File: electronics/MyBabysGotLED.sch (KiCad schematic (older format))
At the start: 16 parts, among them J1 APA102, J2 WS2812, J3 Serial, P3 ATX_Power_2x12_Connector, Q1 PZT2222A, U2 SN74AHCT125, U3 LM1117-3.3

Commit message: Most of BoM details added.  Part of #4
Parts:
- C1: Farnell (none) -> 2326201; Farnell Price/Stock (none) -> https://uk.farnell.com/panasonic/eeefk1e102aq/cap-1000-f-25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
- C3: value 100nF -> 0.1uF; Farnell (none) -> 1759038RL; Farnell Price/Stock (none) -> https://uk.farnell.com/multicomp/mc0603f104z250ct/cap-0-1-f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
- C4: footprint Capacitor_SMD:C_0603_1608Metric_Pad1.05x0.95mm_HandSolder -> Capacitor_SMD:C_1206_3216Metric_Pad1.42x1.75mm_HandSolder; Farnell (none) -> 2320887RL; Farnell Price/Stock (none) -> https://uk.farnell.com/multicomp/mc1206x106k250ct/cap-10-f-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
- C5: Farnell (none) -> 1759038RL; Farnell Price/Stock (none) -> https://uk.farnell.com/multicomp/mc0603f104z250ct/cap-0-1-f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
- F1: Farnell (none) -> 1861167RL; Farnell Price/Stock (none) -> https://uk.farnell.com/multicomp/mc36225/fuse-ptc-reset-smd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
- J3: Description (none) -> DNP
- Q1: value PZT2222A -> NJT4031NT1G; Farnell (none) -> 2533335; Farnell Price/Stock (none) -> https://uk.farnell.com/on-semiconductor/njt4031nt1g/transis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
- R3, R4, R5: Farnell (none) -> 2502462; Farnell Price/Stock (none) -> https://uk.farnell.com/walsin/wr06x4700ftl/res-470r-1-75v-0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
- U2: Farnell (none) -> 3006129; Farnell Price/Stock (none) -> https://uk.farnell.com/texas-instruments/sn74ahct125d/ic-bu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
- U3: Farnell (none) -> 1202826RL; Farnell Price/Stock (none) -> https://uk.farnell.com/stmicroelectronics/ld1117s33tr/v-reg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
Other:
- moved on the sheet: Q1
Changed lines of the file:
@@
 F 2 "Package_SO:SOIC-14_3.9x8.7mm_P1.27mm" H 4250 4600 50  0001 C CNN
 F 3 "https://www.ti.com/lit/ds/symlink/sn74ahct125.pdf" H 4250 4600 50  0001 C CNN
+F 4 "3006129" H 4250 4600 50  0001 C CNN "Farnell"
+F 5 "https://uk.farnell.com/texas-instruments/sn74ahct125d/ic-buffer-gate-quad-3state-smd/dp/3006129" H 4250 4600 50  0001 C CNN "Farnell Price/Stock"
 	1    4250 4600
 	1    0    0    -1
@@
 F 2 "Capacitor_SMD:C_0603_1608Metric_Pad1.05x0.95mm_HandSolder" H 5388 4400 50  0001 C CNN
 F 3 "~" H 5350 4550 50  0001 C CNN
+F 4 "1759038RL" H 5350 4550 50  0001 C CNN "Farnell"
+F 5 "https://uk.farnell.com/multicomp/mc0603f104z250ct/cap-0-1-f-25v-y5v-0603/dp/1759038RL" H 5350 4550 50  0001 C CNN "Farnell Price/Stock"
 	1    5350 4550
 	1    0    0    -1
@@
 F 2 "Resistor_SMD:R_0603_1608Metric_Pad1.05x0.95mm_HandSolder" V 2980 4800 50  0001 C CNN
 F 3 "~" H 3050 4800 50  0001 C CNN
+F 4 "2502462" V 3050 4800 50  0001 C CNN "Farnell"
+F 5 "https://uk.farnell.com/walsin/wr06x4700ftl/res-470r-1-75v-0603-thick-film/dp/2502462" V 3050 4800 50  0001 C CNN "Farnell Price/Stock"
 	1    3050 4800
 	0    1    1    0
@@
 F 2 "Resistor_SMD:R_0603_1608Metric_Pad1.05x0.95mm_HandSolder" V 2980 4500 50  0001 C CNN
 F 3 "~" H 3050 4500 50  0001 C CNN
+F 4 "2502462" V 3050 4500 50  0001 C CNN "Farnell"
+F 5 "https://uk.farnell.com/walsin/wr06x4700ftl/res-470r-1-75v-0603-thick-film/dp/2502462" V 3050 4500 50  0001 C CNN "Farnell Price/Stock"
 	1    3050 4500
 	0    1    1    0
@@
 F 2 "Connector_PinHeader_2.54mm:PinHeader_1x06_P2.54mm_Vertical" H 6650 1150 50  0001 C CNN
 F 3 "~" H 6650 1150 50  0001 C CNN
+F 4 "DNP" H 6650 1150 50  0001 C CNN "Description"
 	1    6650 1150
 	0    -1   -1   0
@@
 F 2 "Package_TO_SOT_SMD:SOT-223-3_TabPin2" H 4550 1800 50  0001 C CNN
 F 3 "http://www.ti.com/lit/ds/symlink/lm1117.pdf" H 4550 1800 50  0001 C CNN
+F 4 "1202826RL" H 4550 1800 50  0001 C CNN "Farnell"
+F 5 "https://uk.farnell.com/stmicroelectronics/ld1117s33tr/v-reg-ldo-3-3v-smd-1117-sot-223/dp/1202826RL" H 4550 1800 50  0001 C CNN "Farnell Price/Stock"
 	1    4550 1800
 	1    0    0    -1
@@
 P 3900 1950
 F 0 "C3" H 4015 1996 50  0000 L CNN
-F 1 "100nF" H 4015 1905 50  0000 L CNN
+F 1 "0.1uF" H 4015 1905 50  0000 L CNN
 F 2 "Capacitor_SMD:C_0603_1608Metric_Pad1.05x0.95mm_HandSolder" H 3938 1800 50  0001 C CNN
 F 3 "~" H 3900 1950 50  0001 C CNN
+F 4 "1759038RL" H 3900 1950 50  0001 C CNN "Farnell"
+F 5 "https://uk.farnell.com/multicomp/mc0603f104z250ct/cap-0-1-f-25v-y5v-0603/dp/1759038RL" H 3900 1950 50  0001 C CNN "Farnell Price/Stock"
 	1    3900 1950
 	1    0    0    -1
@@
 F 0 "C4" H 5215 1996 50  0000 L CNN
 F 1 "10uF" H 5215 1905 50  0000 L CNN
-F 2 "Capacitor_SMD:C_0603_1608Metric_Pad1.05x0.95mm_HandSolder" H 5138 1800 50  0001 C CNN
+F 2 "Capacitor_SMD:C_1206_3216Metric_Pad1.42x1.75mm_HandSolder" H 5138 1800 50  0001 C CNN
 F 3 "~" H 5100 1950 50  0001 C CNN
+F 4 "2320887RL" H 5100 1950 50  0001 C CNN "Farnell"
+F 5 "https://uk.farnell.com/multicomp/mc1206x106k250ct/cap-10-f-25v-10-x5r-1206/dp/2320887RL" H 5100 1950 50  0001 C CNN "Farnell Price/Stock"
 	1    5100 1950
 	1    0    0    -1
@@
 Wire Wire Line
 	3900 2100 3900 2700
-Wire Wire Line
-	3900 2700 3300 2700
 Connection ~ 3900 2100
 Connection ~ 2400 2700
@@
 F 2 "mcqn-kicad-lib:c_elec_12.5x12.5" H 1838 4300 50  0001 C CNN
 F 3 "~" H 1800 4450 50  0001 C CNN
+F 4 "2326201" H 1800 4450 50  0001 C CNN "Farnell"
+F 5 "https://uk.farnell.com/panasonic/eeefk1e102aq/cap-1000-f-25v-radial-smd/dp/2326201" H 1800 4450 50  0001 C CNN "Farnell Price/Stock"
 	1    1800 4450
 	1    0    0    -1
@@
 F 2 "Resistor_SMD:R_0603_1608Metric_Pad1.05x0.95mm_HandSolder" V 4280 2400 50  0001 C CNN
 F 3 "~" H 4350 2400 50  0001 C CNN
+F 4 "2502462" V 4350 2400 50  0001 C CNN "Farnell"
+F 5 "https://uk.farnell.com/walsin/wr06x4700ftl/res-470r-1-75v-0603-thick-film/dp/2502462" V 4350 2400 50  0001 C CNN "Farnell Price/Stock"
 	1    4350 2400
 	0    1    1    0
@@
 L Transistor_BJT:PZT2222A Q1
 U 1 1 5F963FC6
-P 3400 2400
-F 0 "Q1" H 3591 2446 50  0000 L CNN
-F 1 "PZT2222A" H 3591 2355 50  0000 L CNN
-F 2 "Package_TO_SOT_SMD:SOT-223-3_TabPin2" H 3600 2325 50  0001 L CIN
-F 3 "http://www.fairchildsemi.com/ds/PN/PN2222A.pdf" H 3400 2400 50  0001 L CNN
-	1    3400 2400
+P 3550 2400
+F 0 "Q1" H 3741 2446 50  0000 L CNN
+F 1 "NJT4031NT1G" H 3741 2355 50  0000 L CNN
+F 2 "Package_TO_SOT_SMD:SOT-223-3_TabPin2" H 3750 2325 50  0001 L CIN
+F 3 "http://www.fairchildsemi.com/ds/PN/PN2222A.pdf" H 3550 2400 50  0001 L CNN
+F 4 "2533335" H 3550 2400 50  0001 C CNN "Farnell"
+F 5 "https://uk.farnell.com/on-semiconductor/njt4031nt1g/transistor-bipol-npn-40v/dp/2533335" H 3550 2400 50  0001 C CNN "Farnell Price/Stock"
+	1    3550 2400
 	-1   0    0    -1
 $EndComp
-Wire Wire Line
-	2850 2100 3300 2100
-Wire Wire Line
-	3300 2100 3300 2200
-Wire Wire Line
-	3300 2600 3300 2700
-Connection ~ 3300 2700
-Wire Wire Line
-	3300 2700 2400 2700
-Wire Wire Line
-	3600 2400 4200 2400
 Wire Wire Line
 	4500 2400 7950 2400
@@
 F 2 "Fuse:Fuse_1812_4532Metric_Pad1.30x3.40mm_HandSolder" H 3350 1600 50  0001 L CNN
 F 3 "~" H 3300 1800 50  0001 C CNN
+F 4 "1861167RL" V 3300 1800 50  0001 C CNN "Farnell"
+F 5 "https://uk.farnell.com/multicomp/mc36225/fuse-ptc-reset-smd-24v-1-1a/dp/1861167RL" V 3300 1800 50  0001 C CNN "Farnell Price/Stock"
 	1    3300 1800
 	0    1    1    0
@@
 Wire Wire Line
 	3050 1800 3150 1800
+Wire Wire Line
+	2400 2700 3450 2700
+Wire Wire Line
+	4200 2400 3750 2400
+Wire Wire Line
+	3450 2200 3450 2100
+Wire Wire Line
+	2850 2100 3450 2100
+Wire Wire Line
+	3450 2600 3450 2700
+Connection ~ 3450 2700
+Wire Wire Line
+	3450 2700 3900 2700
 $EndSCHEMATC

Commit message: PCB laid out.  Final part of #3 and all of #5
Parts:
- F2: footprint (none) -> mcqn-kicad-lib:Keystone_3557-2_Blade_Fuseholder; Digikey (none) -> 36-3557-2-ND; Digikey Price/Stock (none) -> https://www.digikey.co.uk/product-detail/en/keystone-electr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; Farnell (none) -> 2292904; Farnell Price/Stock (none) -> https://uk.farnell.com/keystone/3557-2/fuse-holder-0-8x2-8m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
- J1: footprint Connector_Phoenix_MSTB:PhoenixContact_MSTBVA_2,5_5-G-5,08_1x05_P5.08mm_Vertical -> Connector_Phoenix_MSTB:PhoenixContact_MSTBVA_2,5_4-G-5,08_1x04_P5.08mm_Vertical
- J2: footprint (none) -> Connector_PinHeader_2.54mm:PinHeader_1x03_P2.54mm_Vertical; Farnell (none) -> 1593412; Farnell Price/Stock (none) -> https://uk.farnell.com/multicomp/2211s-03g/header-1-row-ver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
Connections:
- net GND: now also J1.1 (Pin_1); no longer J1.4 (Pin_4)
- net LED_Clk: now also U2.2 (1A); no longer U2.5 (2A)
- net LED_Data: now also U2.5 (2A); no longer U2.2 (1A)
- net at C1.1, C5.1, F2.2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: now also J1.4 (Pin_4); no longer J1.1 (Pin_1)
- net at J1.2 (Pin_2), J2.2 (Pin_2): now also R4.2; no longer R3.2
- net at J1.3 (Pin_3): now also R3.2; no longer R4.2
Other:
- moved on the sheet: C1, J2
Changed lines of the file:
@@
 L Connector_Generic:Conn_01x03 J2
 U 1 1 5F8EED32
-P 2350 4500
-F 0 "J2" H 2268 4817 50  0000 C CNN
-F 1 "WS2812" H 2268 4726 50  0000 C CNN
-F 2 "" H 2350 4500 50  0001 C CNN
-F 3 "~" H 2350 4500 50  0001 C CNN
-	1    2350 4500
+P 2350 4800
+F 0 "J2" H 2268 5117 50  0000 C CNN
+F 1 "WS2812" H 2268 5026 50  0000 C CNN
+F 2 "Connector_PinHeader_2.54mm:PinHeader_1x03_P2.54mm_Vertical" H 2350 4800 50  0001 C CNN
+F 3 "~" H 2350 4800 50  0001 C CNN
+F 4 "1593412" H 2350 4800 50  0001 C CNN "Farnell"
+F 5 "https://uk.farnell.com/multicomp/2211s-03g/header-1-row-vert-3way/dp/1593412" H 2350 4800 50  0001 C CNN "Farnell Price/Stock"
+	1    2350 4800
 	-1   0    0    -1
 $EndComp
-$Comp
-L Connector_Generic:Conn_01x04 J1
-U 1 1 5F8F55BB
-P 1200 4500
-F 0 "J1" H 1118 4817 50  0000 C CNN
-F 1 "APA102" H 1118 4726 50  0000 C CNN
-F 2 "Connector_Phoenix_MSTB:PhoenixContact_MSTBVA_2,5_5-G-5,08_1x05_P5.08mm_Vertical" H 1200 4500 50  0001 C CNN
-F 3 "~" H 1200 4500 50  0001 C CNN
-F 4 "2517880" H 1200 4500 50  0001 C CNN "Farnell"
-F 5 "https://uk.farnell.com/imo-precision-controls/21-95mv-4-e/terminal-block-header-4pos-th/dp/2517880" H 1200 4500 50  0001 C CNN "Farnell Price/Stock"
-	1    1200 4500
-	-1   0    0    -1
-$EndComp
-Wire Wire Line
-	2800 3900 2800 4400
-Wire Wire Line
-	2800 4400 2550 4400
 Wire Wire Line
 	1600 3900 1600 4400
@@
 	1600 4400 1400 4400
 Wire Wire Line
-	2550 4500 2800 4500
-Wire Wire Line
 	1400 4600 1500 4600
-Wire Wire Line
-	1500 4600 1500 4800
-Wire Wire Line
-	1400 4500 1600 4500
-Wire Wire Line
-	1600 4500 1600 4700
-Wire Wire Line
-	2800 4700 2800 4500
 $Comp
 L Device:C C5
@@
 $EndComp
 Wire Wire Line
-	2800 4500 2900 4500
-Connection ~ 2800 4500
-Wire Wire Line
 	1400 4700 1400 5200
 Wire Wire Line
@@
 	5350 3900 5350 4300
 Connection ~ 5350 4300
-Wire Wire Line
-	2550 4600 2550 5200
 Wire Wire Line
 	3900 4300 3800 4300
@@
 U 1 1 5F90A6A8
 P 4550 1800
+AR Path="/5F90A6A8" Ref="U3"  Part="1"
+AR Path="/5F8DAD46/5F90A6A8" Ref="U3"  Part="1"
 F 0 "U3" H 4550 2042 50  0000 C CNN
 F 1 "LM1117-3.3" H 4550 1951 50  0000 C CNN
@@
 L Device:CP C1
 U 1 1 5F942FA9
-P 1800 4450
-F 0 "C1" H 1918 4496 50  0000 L CNN
-F 1 "1000uF" H 1918 4405 50  0000 L CNN
-F 2 "mcqn-kicad-lib:c_elec_12.5x12.5" H 1838 4300 50  0001 C CNN
-F 3 "~" H 1800 4450 50  0001 C CNN
-F 4 "2326201" H 1800 4450 50  0001 C CNN "Farnell"
-F 5 "https://uk.farnell.com/panasonic/eeefk1e102aq/cap-1000-f-25v-radial-smd/dp/2326201" H 1800 4450 50  0001 C CNN "Farnell Price/Stock"
-	1    1800 4450
-	1    0    0    -1
-$EndComp
-Wire Wire Line
-	1600 3900 1800 3900
-Wire Wire Line
-	1600 4700 2800 4700
-Wire Wire Line
-	1500 4800 2900 4800
-Wire Wire Line
-	1400 5200 1800 5200
-Connection ~ 1800 3900
-Wire Wire Line
-	1800 3900 2800 3900
-Wire Wire Line
-	1800 3900 1800 4300
-Wire Wire Line
-	1800 4600 1800 5200
-Connection ~ 1800 5200
-Wire Wire Line
-	1800 5200 2550 5200
+P 1850 4250
+F 0 "C1" H 1968 4296 50  0000 L CNN
+F 1 "1000uF" H 1968 4205 50  0000 L CNN
+F 2 "mcqn-kicad-lib:c_elec_12.5x12.5" H 1888 4100 50  0001 C CNN
+F 3 "~" H 1850 4250 50  0001 C CNN
+F 4 "2326201" H 1850 4250 50  0001 C CNN "Farnell"
+F 5 "https://uk.farnell.com/panasonic/eeefk1e102aq/cap-1000-f-25v-radial-smd/dp/2326201" H 1850 4250 50  0001 C CNN "Farnell Price/Stock"
+	1    1850 4250
+	1    0    0    -1
+$EndComp
 $Comp
 L Device:R R5
@@
 Wire Wire Line
 	3200 4500 3900 4500
-Connection ~ 2800 3900
 $Comp
 L Device:Fuse F2
@@
 F 0 "F2" H 4910 3696 50  0000 L CNN
 F 1 "Fuse" H 4910 3605 50  0000 L CNN
-F 2 "" V 4780 3650 50  0001 C CNN
+F 2 "mcqn-kicad-lib:Keystone_3557-2_Blade_Fuseholder" V 4780 3650 50  0001 C CNN
 F 3 "~" H 4850 3650 50  0001 C CNN
+F 4 "2292904" H 4850 3650 50  0001 C CNN "Farnell"
+F 5 "https://uk.farnell.com/keystone/3557-2/fuse-holder-0-8x2-8mm-pcb-mount/dp/2292904" H 4850 3650 50  0001 C CNN "Farnell Price/Stock"
+F 6 "36-3557-2-ND" H 4850 3650 50  0001 C CNN "Digikey"
+F 7 "https://www.digikey.co.uk/product-detail/en/keystone-electronics/3557-2/36-3557-2-ND/2137305" H 4850 3650 50  0001 C CNN "Digikey Price/Stock"
 	1    4850 3650
 	1    0    0    -1
 $EndComp
-Wire Wire Line
-	2800 3900 4850 3900
 Wire Wire Line
 	4850 3400 4850 3500
@@
 Text GLabel 8500 2600 0    50   Input ~ 0
 LED_Data
+Text GLabel 3700 4700 0    50   Input ~ 0
+LED_Data
 Text GLabel 3700 4400 0    50   Input ~ 0
-LED_Data
-Text GLabel 3700 4700 0    50   Input ~ 0
 LED_Clk
 $Comp
@@
 Wire Wire Line
 	3450 2700 3900 2700
+Wire Wire Line
+	1400 5200 1850 5200
+Wire Wire Line
+	2550 4900 2550 5200
+Wire Wire Line
+	2550 4800 2750 4800
+Wire Wire Line
+	1400 4500 2900 4500
+Wire Wire Line
+	2550 3900 2550 4700
+Connection ~ 2550 3900
+Wire Wire Line
+	2550 3900 4850 3900
+Wire Wire Line
+	1600 3900 1850 3900
+Wire Wire Line
+	1850 4100 1850 3900
+Connection ~ 1850 3900
+Wire Wire Line
+	1850 3900 2550 3900
+Wire Wire Line
+	1850 4400 1850 5200
+Connection ~ 1850 5200
+Wire Wire Line
+	1850 5200 2550 5200
+Wire Wire Line
+	1500 5050 2750 5050
+Wire Wire Line
+	2750 5050 2750 4800
+Wire Wire Line
+	1500 4600 1500 5050
+Connection ~ 2750 4800
+Wire Wire Line
+	2750 4800 2900 4800
+$Comp
+L Connector_Generic:Conn_01x04 J1
+U 1 1 5F8F55BB
+P 1200 4600
+F 0 "J1" H 1118 4917 50  0000 C CNN
+F 1 "APA102" H 1118 4826 50  0000 C CNN
+F 2 "Connector_Phoenix_MSTB:PhoenixContact_MSTBVA_2,5_4-G-5,08_1x04_P5.08mm_Vertical" H 1200 4600 50  0001 C CNN
+F 3 "~" H 1200 4600 50  0001 C CNN
+F 4 "2517880" H 1200 4600 50  0001 C CNN "Farnell"
+F 5 "https://uk.farnell.com/imo-precision-controls/21-95mv-4-e/terminal-block-header-4pos-th/dp/2517880" H 1200 4600 50  0001 C CNN "Farnell Price/Stock"
+	1    1200 4600
+	-1   0    0    1
+$EndComp
 $EndSCHEMATC

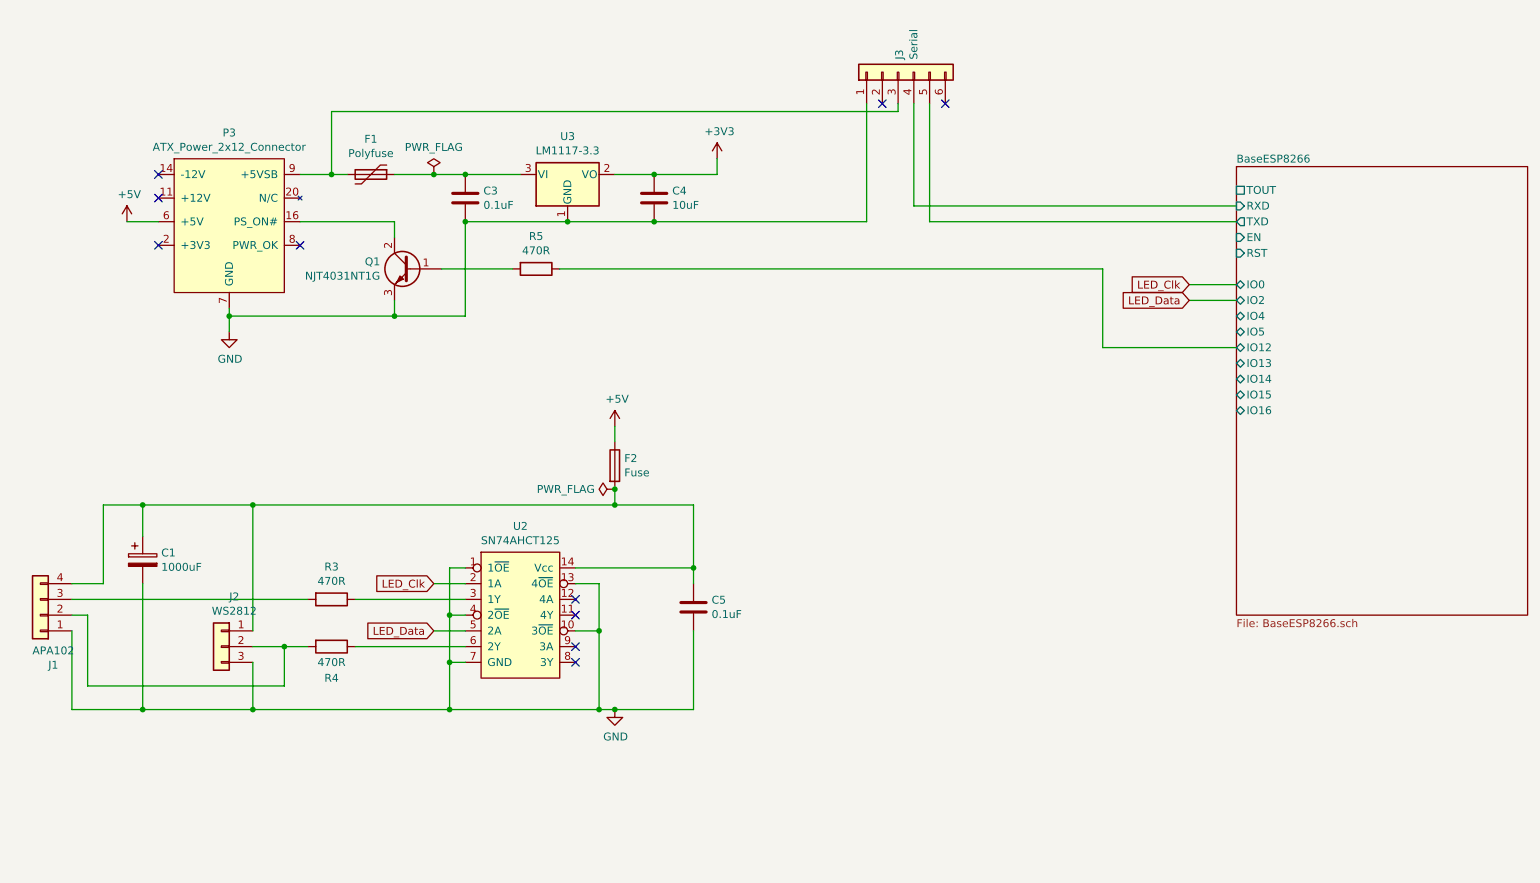
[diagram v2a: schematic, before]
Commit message: Board mods to use lower value fuses (rather than a single large fuse).  Fixes #14
* Three 5V/Gnd feeds rather than one, each protected with a 5x20mm 8A fuse
* 470uF smoothing caps on the 5V lines, rather than a single 1000uF
* New test points for 5V, data and clock lines
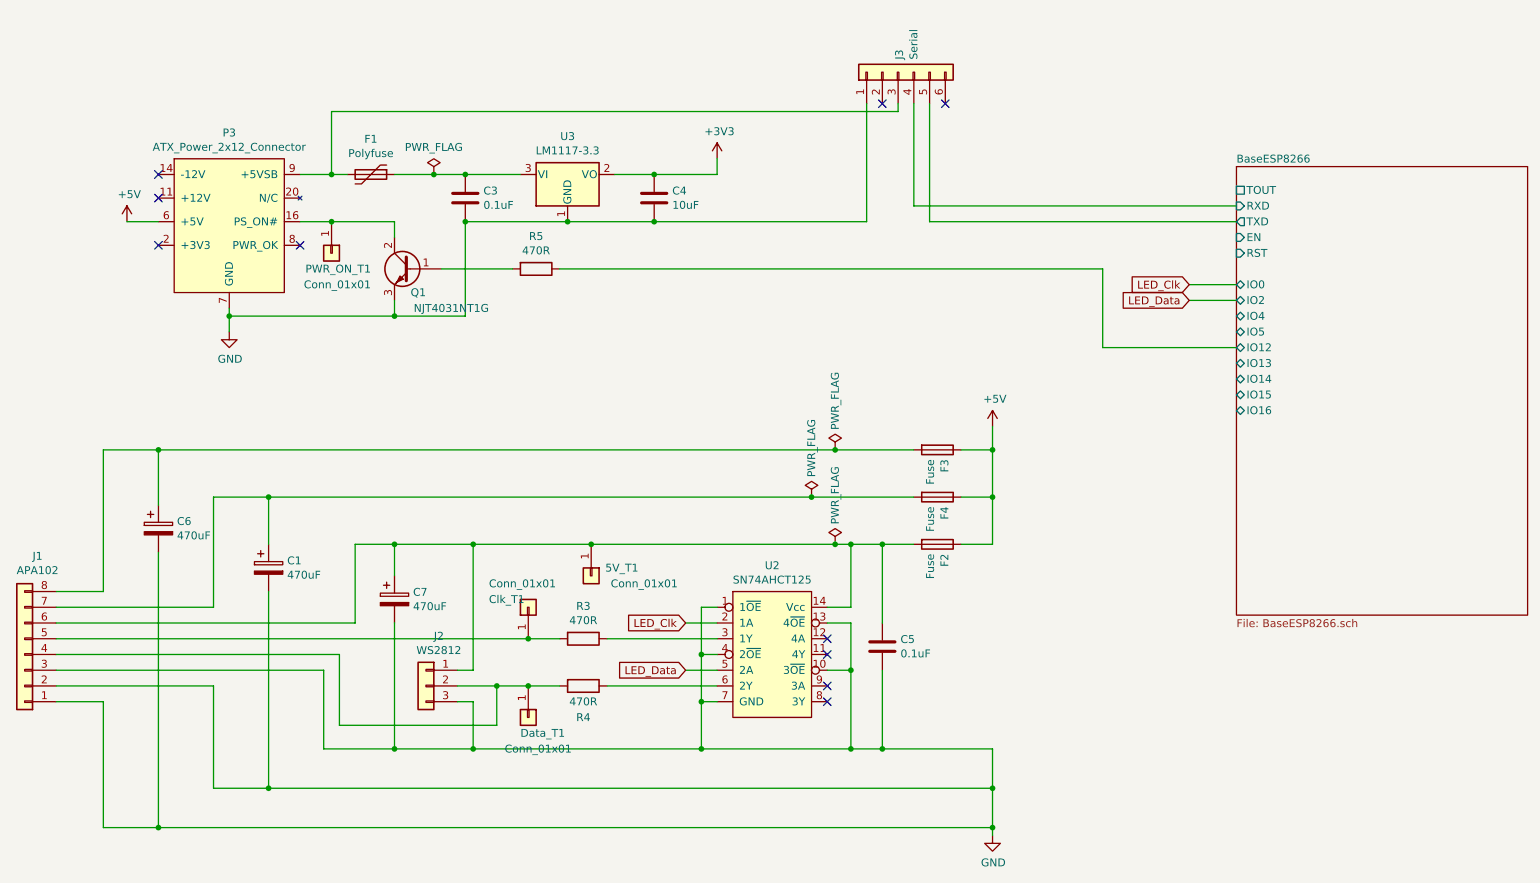
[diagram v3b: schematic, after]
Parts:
- removed J1: APA102, Connector_Phoenix_MSTB:PhoenixContact_MSTBVA_2,5_4-G-5,08_1x04_P5.08mm_Vertical, symbol Connector_Generic:Conn_01x04
- added 5V_T1, Clk_T1, Data_T1, PWR_ON_T1: Conn_01x01, TestPoint:TestPoint_Pad_D2.0mm, symbol Connector_Generic:Conn_01x01
- added C6, C7: 470uF, Capacitor_SMD:C_Elec_10x10.2, symbol Device:CP
- added F3, F4: Fuse, mcqn-kicad-lib:Fuseholder_Cylinder-5x20mm_Wurth_WR-FSH_Horizontal, symbol Device:Fuse
- added J1: APA102, Connector_Phoenix_MSTB:PhoenixContact_MSTBVA_2,5_8-G-5,08_1x08_P5.08mm_Vertical, symbol Connector_Generic:Conn_01x08
- C1: value 1000uF -> 470uF; footprint mcqn-kicad-lib:c_elec_12.5x12.5 -> Capacitor_SMD:C_Elec_10x10.2; Farnell 2326201 -> 2254313; Farnell Price/Stock https://uk.farnell.com/panasonic/eeefk1e102aq/cap-1000-f-25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 -> https://uk.farnell.com/panasonic/eeefc1e471p/cap-470-f-25v-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
- F2: footprint mcqn-kicad-lib:Keystone_3557-2_Blade_Fuseholder -> mcqn-kicad-lib:Fuseholder_Cylinder-5x20mm_Wurth_WR-FSH_Horizontal; Digikey 36-3557-2-ND -> (none); Digikey Price/Stock https://www.digikey.co.uk/product-detail/en/keystone-electr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 -> (none); Farnell 2292904 -> 2471681; Farnell Price/Stock https://uk.farnell.com/keystone/3557-2/fuse-holder-0-8x2-8m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 -> https://uk.farnell.com/wurth-elektronik/696107003002/fuse-h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
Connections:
- net +5V: now also F3.1, F4.1
- net GND: now also C6.2, C7.2, J1.1 (Pin_1), J1.2 (Pin_2), J1.3 (Pin_3)
- net at C5.1, F2.2, J2.1 (Pin_1)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: now also 5V_T1.1 (Pin_1), C7.1, J1.6 (Pin_6); no longer C1.1
- net at P3.16 (PS_ON#), Q1.2 (C): now also PWR_ON_T1.1 (Pin_1)
- net at J2.2 (Pin_2), R4.2: now also Data_T1.1 (Pin_1), J1.4 (Pin_4)
- net at R3.2: now also Clk_T1.1 (Pin_1), J1.5 (Pin_5)
- new net: C1.1, F4.2, J1.7 (Pin_7)
- new net: C6.1, F3.2, J1.8 (Pin_8)
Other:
- moved on the sheet: C1, C5, F2, J2, R3, R4, U2

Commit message: Correct Farnell part number for the terminal block
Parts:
- J1: Farnell 2517880 -> 2517883
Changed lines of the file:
@@
 F 2 "Connector_Phoenix_MSTB:PhoenixContact_MSTBVA_2,5_8-G-5,08_1x08_P5.08mm_Vertical" H 1100 4850 50  0001 C CNN
 F 3 "~" H 1100 4850 50  0001 C CNN
-F 4 "2517880" H 1100 4850 50  0001 C CNN "Farnell"
+F 4 "2517883" H 1100 4850 50  0001 C CNN "Farnell"
 F 5 "https://uk.farnell.com/imo-precision-controls/21-95mv-8-e/terminal-block-header-8pos-th/dp/2517883" H 1100 4850 50  0001 C CNN "Farnell Price/Stock"
 	1    1100 4850
